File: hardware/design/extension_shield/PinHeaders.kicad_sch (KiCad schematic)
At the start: 6 parts, among them J1 SSQ-108-XX-X-D, J2 SSQ-110-03-T-D, J3 SSQ-108-XX-X-D, J4 SSQ-106-03-T-D, J8 SSQ-114-03-T-D, J9 SSQ-116-XX-X-D

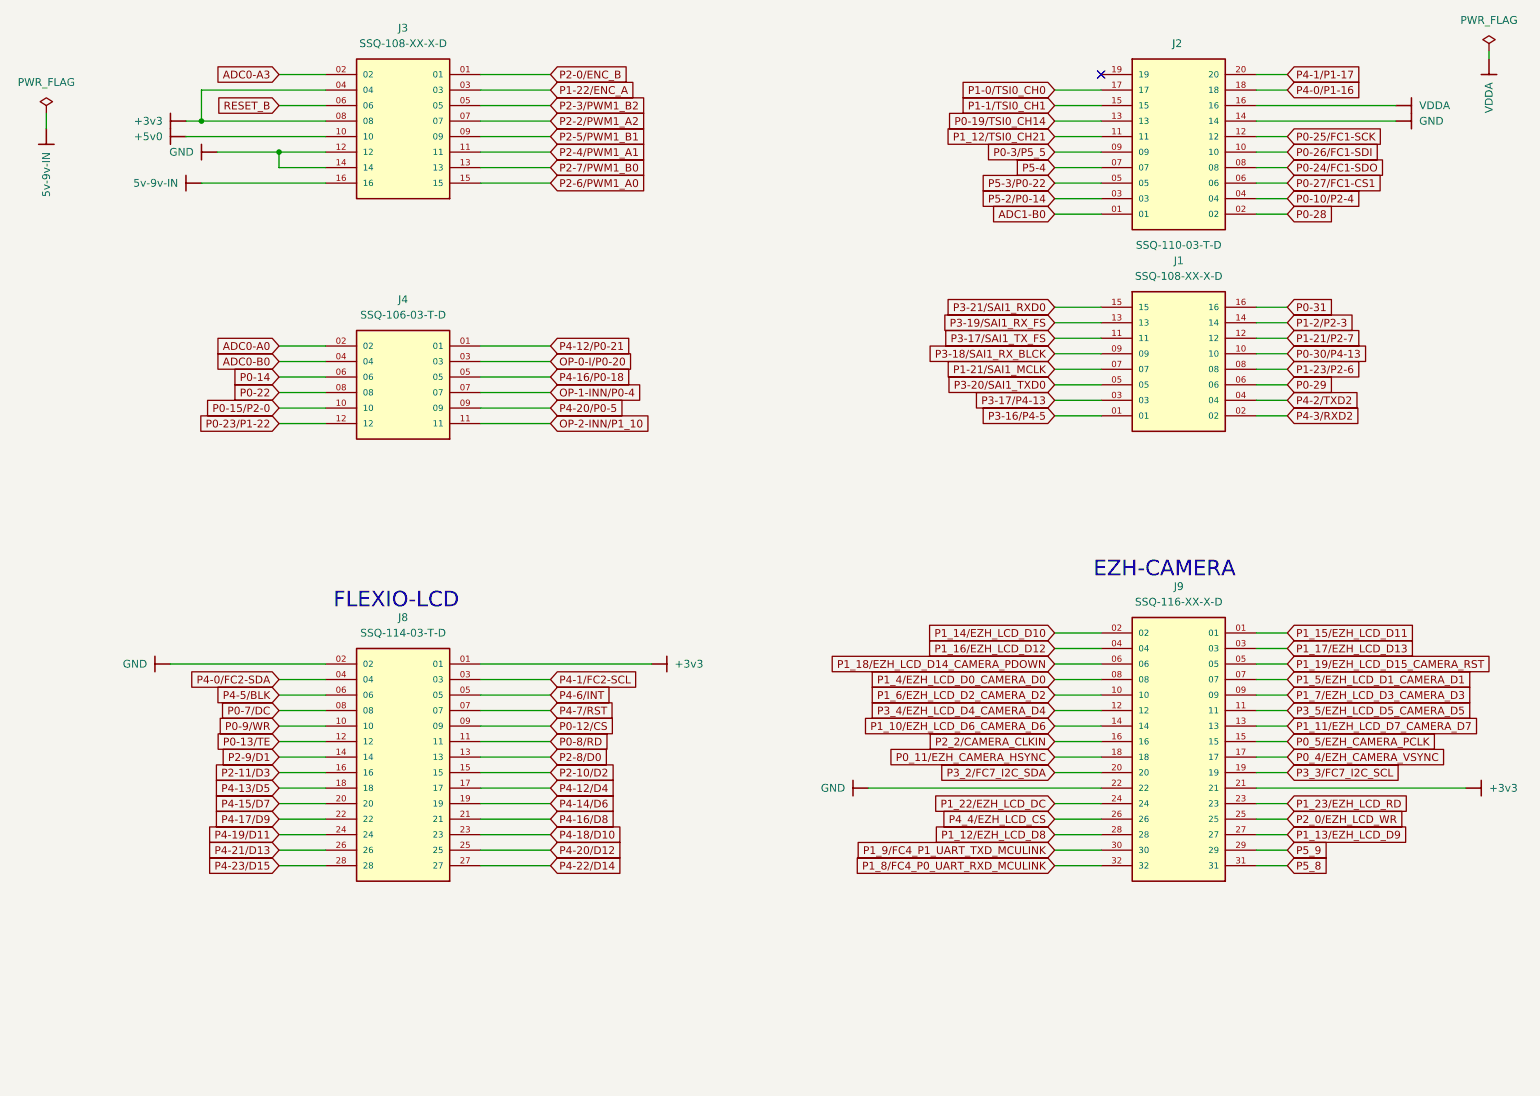
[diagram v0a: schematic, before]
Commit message: [HW/SHIELD] Adds Genereated PDF Schematic & Newer Version of Expansion Shield.
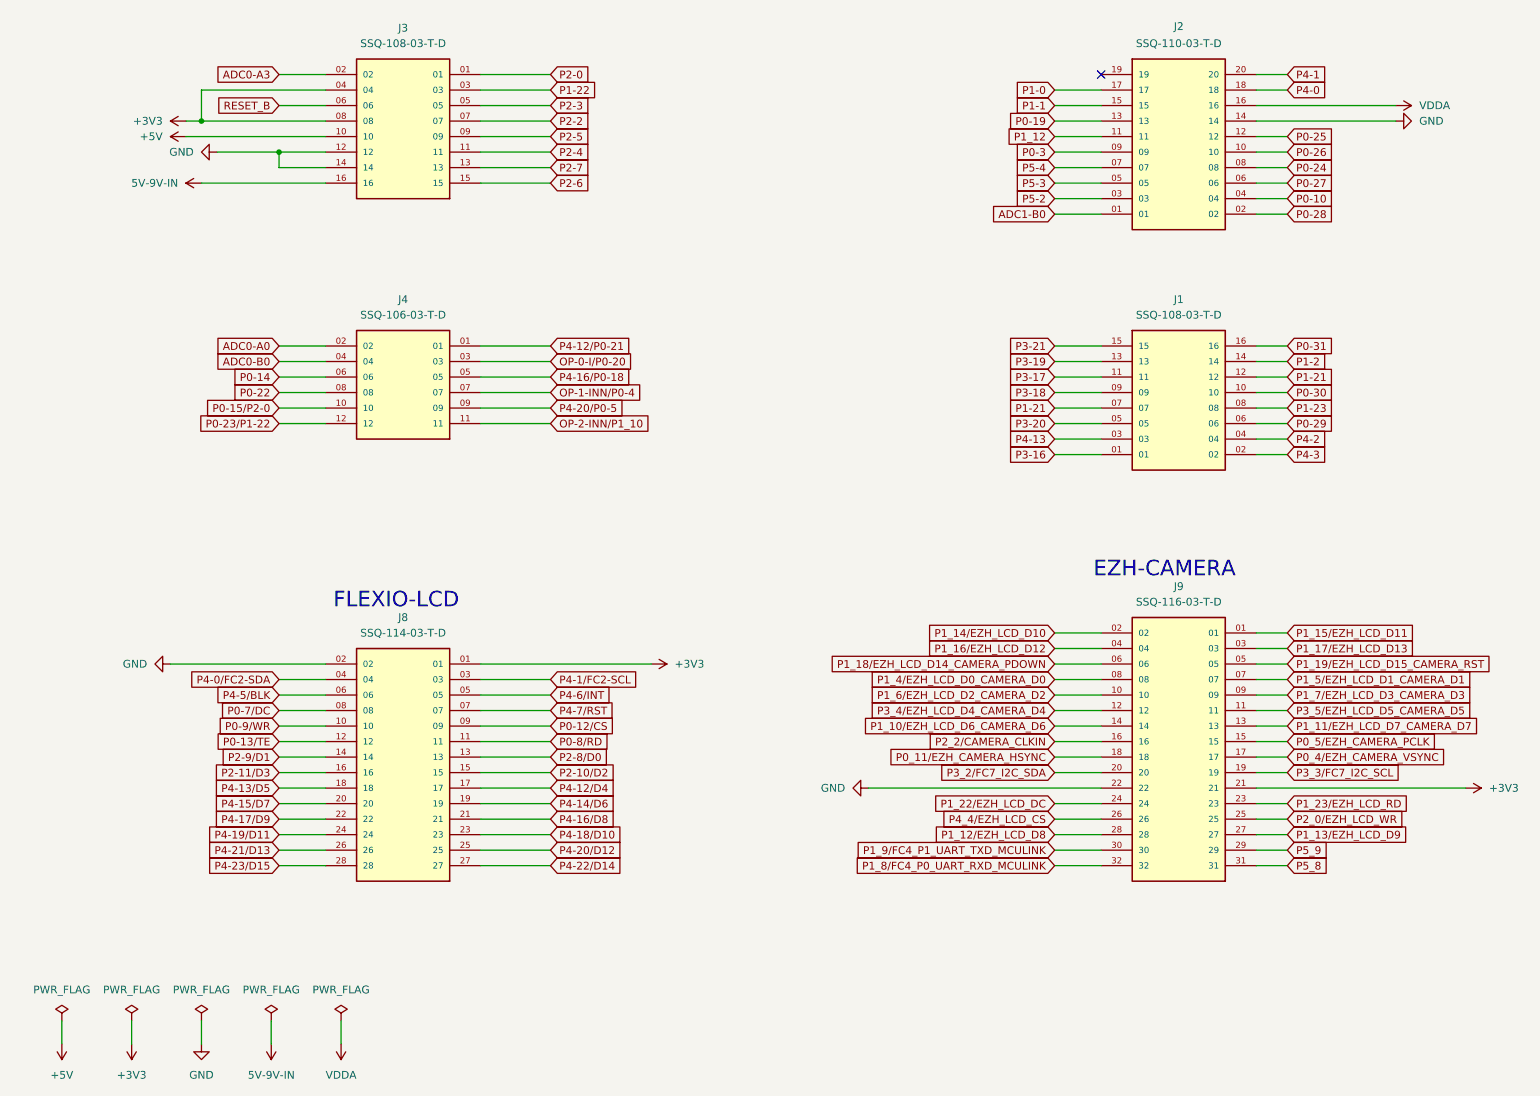
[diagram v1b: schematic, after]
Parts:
- J1, J3: value SSQ-108-XX-X-D -> SSQ-108-03-T-D
- J9: value SSQ-116-XX-X-D -> SSQ-116-03-T-D
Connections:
- net P1-21/SAI1_MCLK is gone; now on net P1-21: J1.07
- net +3v3 renamed +3V3
- net +5v0 renamed +5V
- net 5v-9v-IN renamed 5V-9V-IN
- net P0-10/P2-4 renamed P0-10
- net P0-19/TSI0_CH14 renamed P0-19
- net P0-24/FC1-SDO renamed P0-24
- net P0-25/FC1-SCK renamed P0-25
- net P0-26/FC1-SDI renamed P0-26
- net P0-27/FC1-CS1 renamed P0-27
- net P0-30/P4-13 renamed P0-30
- net P0-3/P5_5 renamed P0-3
- net P1-0/TSI0_CH0 renamed P1-0
- net P1-1/TSI0_CH1 renamed P1-1
- net P1-21/P2-7 renamed P1-21
- net P1-22/ENC_A renamed P1-22
- net P1-23/P2-6 renamed P1-23
- net P1-2/P2-3 renamed P1-2
- net P1_12/TSI0_CH21 renamed P1_12
- net P2-0/ENC_B renamed P2-0
- net P2-2/PWM1_A2 renamed P2-2
- net P2-3/PWM1_B2 renamed P2-3
- net P2-4/PWM1_A1 renamed P2-4
- net P2-5/PWM1_B1 renamed P2-5
- net P2-6/PWM1_A0 renamed P2-6
- net P2-7/PWM1_B0 renamed P2-7
- net P3-16/P4-5 renamed P3-16
- net P3-17/P4-13 renamed P4-13
- net P3-17/SAI1_TX_FS renamed P3-17
- net P3-18/SAI1_RX_BLCK renamed P3-18
- net P3-19/SAI1_RX_FS renamed P3-19
- net P3-20/SAI1_TXD0 renamed P3-20
- net P3-21/SAI1_RXD0 renamed P3-21
- net P4-0/P1-16 renamed P4-0
- net P4-1/P1-17 renamed P4-1
- net P4-2/TXD2 renamed P4-2
- net P4-3/RXD2 renamed P4-3
- net P5-2/P0-14 renamed P5-2
- net P5-3/P0-22 renamed P5-3
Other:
- title: (none) -> Datalogger Expansion Shield
- moved on the sheet: J1
